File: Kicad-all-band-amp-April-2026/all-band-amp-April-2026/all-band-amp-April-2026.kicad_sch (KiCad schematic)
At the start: 120 parts, among them J1 SWR1, J10 Aux In, J11 LPF, J12 Digi In/Out, J13 12v/5v Outputs, J14 TX2/RX2, J15 TX0/RX0, J16 50v In., J17 PWM Out, J18 PTT IN, J19 DISPLAY POWER, J2 SWR2, J20 5V Output, J22 UDPI, J23 12v Output, J24 12v Output, J25 Temp 2, J26 Power Link, J3 I opt Input, J4 RF In Level, J5 50v In., J6 Temp, J7 Conn_01x03_Pin, J8 12v Input, J9 I2c Output, Q1 2n2222, Q2 2n2222, U1 LTV-847, U2 MCP23017_SP, U3 LM393, U4 MIC2981/82YN, U5 MIC2981/82YN, U6 R-78E5.0-1.0, U8 LTV-827, U9 ACS712xLCTR-30A

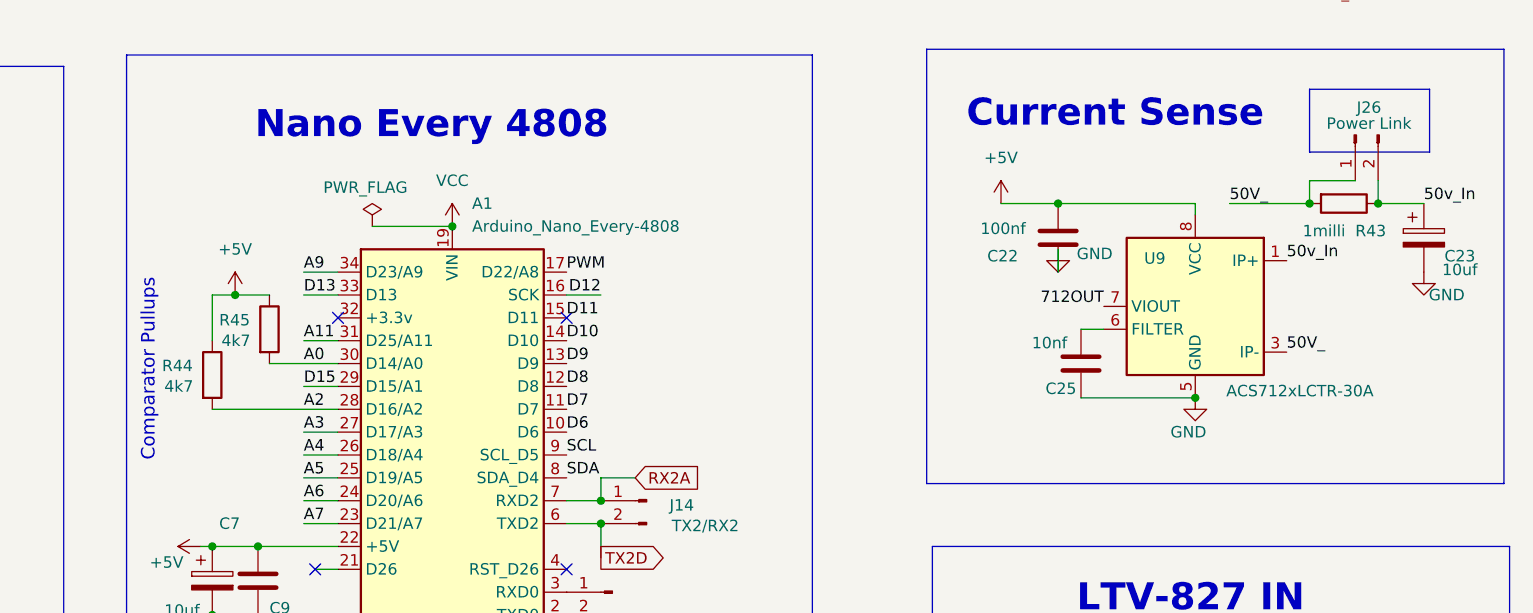
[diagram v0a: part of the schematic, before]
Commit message: change componet values
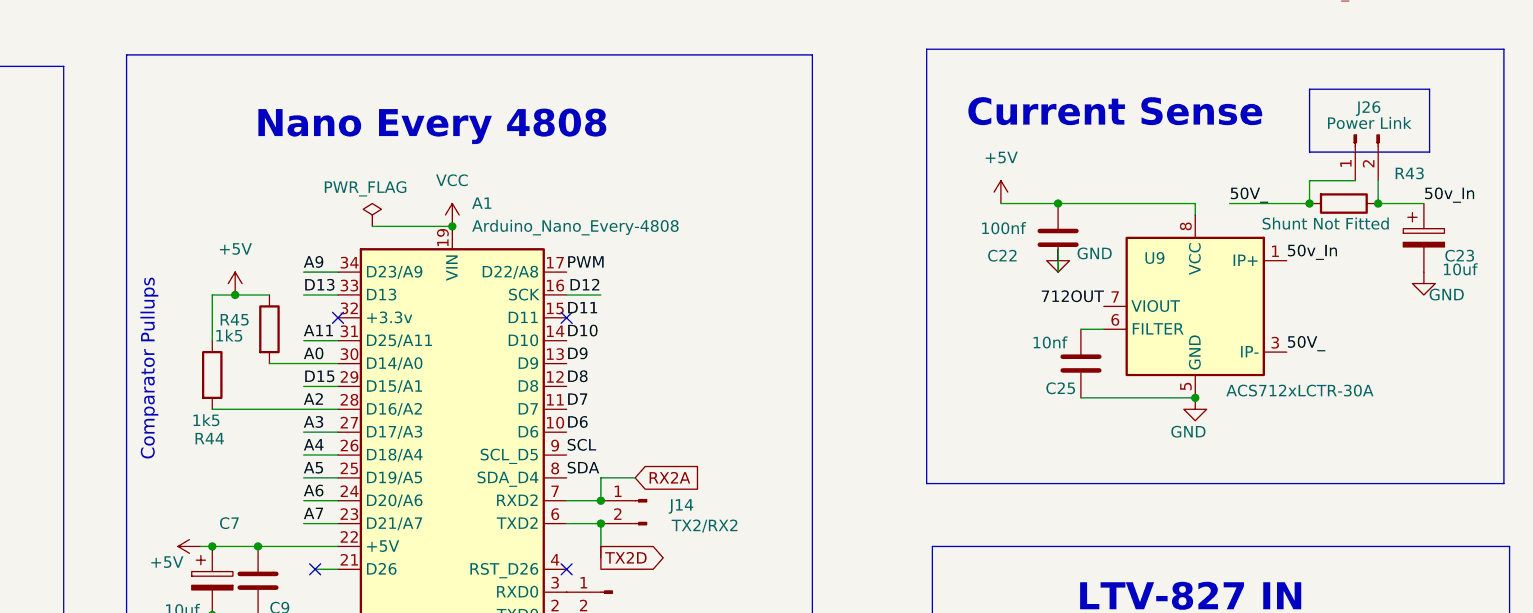
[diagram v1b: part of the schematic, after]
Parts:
- R43: value 1milli -> Shunt Not Fitted
- R44, R45: value 4k7 -> 1k5
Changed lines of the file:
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@@
 		(dnp no)
 		(property "Reference" "R44"
-			(at 252.222 87.884 0)
+			(at 255.778 96.012 0)
 			(effects
 				(font
@@
 			)
 		)
-		(property "Value" "4k7"
-			(at 252.476 90.17 0)
+		(property "Value" "1k5"
+			(at 255.524 93.98 0)
 			(effects
 				(font
@@
 			)
 		)
-		(property "Value" "4k7"
-			(at 258.826 85.09 0)
+		(property "Value" "1k5"
+			(at 258.064 84.582 0)
 			(effects
 				(font
@@
 		(dnp no)
 		(property "Reference" "R43"
-			(at 384.81 72.898 90)
+			(at 389.128 66.548 90)
 			(effects
 				(font
@@
 			)
 		)
-		(property "Value" "1milli"
-			(at 378.968 72.898 90)
+		(property "Value" "Shunt Not Fitted"
+			(at 374.396 72.136 90)
 			(effects
 				(font

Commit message: update functions
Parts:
- R3, R7: value 1k5 -> 1k5-3k3
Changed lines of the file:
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@@
 			)
 		)
-		(property "Value" "1k5"
-			(at 35.56 130.048 0)
+		(property "Value" "1k5-3k3"
+			(at 43.18 129.54 0)
 			(effects
 				(font
@@
 		(dnp no)
 		(property "Reference" "R7"
-			(at 36.83 175.006 0)
-			(effects
-				(font
-					(size 1.27 1.27)
-				)
-				(justify left)
-			)
-		)
-		(property "Value" "1k5"
-			(at 35.306 176.784 0)
-			(effects
-				(font
+			(at 36.576 176.53 0)
+			(effects
+				(font
+					(size 1.27 1.27)
+				)
+				(justify left)
+			)
+		)
+		(property "Value" "1k5-3k3"
+			(at 42.672 176.276 0)
+			(effects
+				(font

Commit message: improve display
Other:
- note added: "Note: Ensure only DC is applied to the RF in (drive) input. use a low pass filter. Dont let rf into the board!"
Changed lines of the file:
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@@
+		)
+	)
+	(text "Note: \nEnsure only DC is applied \nto the RF in (drive) input.\nuse a low pass filter.\nDont let rf into the board! "
+		(exclude_from_sim no)
+		(at 48.768 38.1 0)
+		(effects
+			(font
+				(size 3 3)
+				(thickness 0.6)
+				(bold yes)
+			)
 		)
 	)

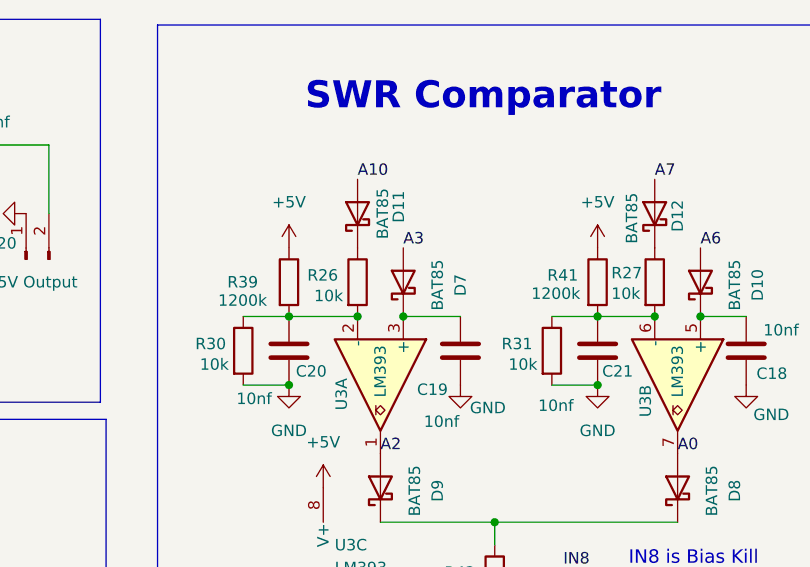
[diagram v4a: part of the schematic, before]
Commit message: update component values
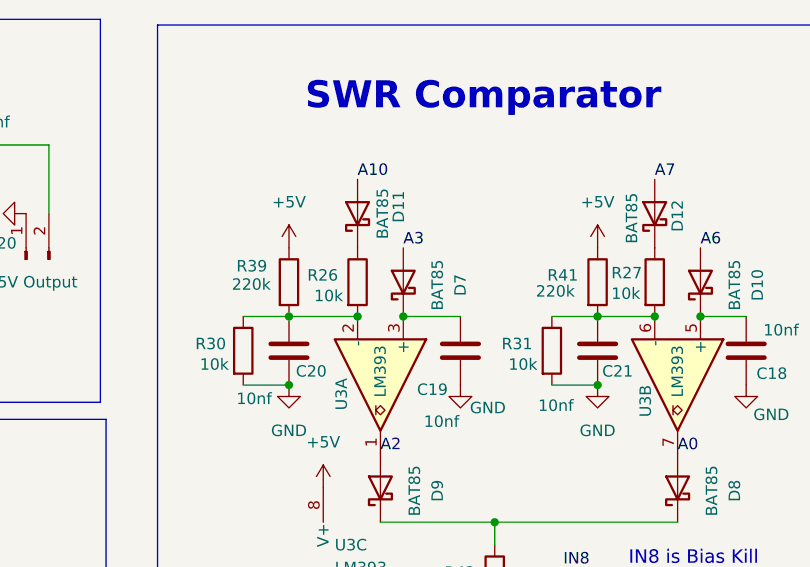
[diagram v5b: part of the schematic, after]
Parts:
- R39, R41: value 1200k -> 220k
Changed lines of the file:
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@@
 			)
 		)
-		(property "Value" "1200k"
-			(at 284.734 182.88 0)
+		(property "Value" "220k"
+			(at 285.242 182.626 0)
 			(show_name no)
 			(do_not_autoplace no)
@@
 		(dnp no)
 		(property "Reference" "R39"
-			(at 250.952 181.61 0)
+			(at 251.968 179.832 0)
 			(show_name no)
 			(do_not_autoplace no)
@@
 			)
 		)
-		(property "Value" "1200k"
-			(at 249.936 183.642 0)
+		(property "Value" "220k"
+			(at 251.46 181.864 0)
 			(show_name no)
 			(do_not_autoplace no)

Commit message: change some values - alter boards
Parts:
- R24, R25: value 10k -> 4k7
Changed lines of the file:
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@@
 			)
 		)
-		(property "Value" "10k"
+		(property "Value" "4k7"
 			(at 144.526 76.708 0)
 			(show_name no)
@@
 			)
 		)
-		(property "Value" "10k"
+		(property "Value" "4k7"
 			(at 131.826 78.74 0)
 			(show_name no)

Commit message: update pcb's
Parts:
- added C26: 10nf, Capacitor_THT:C_Disc_D3.4mm_W2.1mm_P2.50mm, symbol Device:C
- added J27: SWR trip out, Connector_JST:JST_EH_B2B-EH-A_1x02_P2.50mm_Vertical, symbol Connector:Conn_01x02_Pin
- added R46: 1k5, Resistor_THT:R_Axial_DIN0207_L6.3mm_D2.5mm_P7.62mm_Horizontal, symbol Device:R
- added R47: 1k, Resistor_THT:R_Axial_DIN0207_L6.3mm_D2.5mm_P7.62mm_Horizontal, symbol Device:R
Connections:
- net GND: now also C26.2, J27.1 (Pin_1), R47.2
- net SWR: now reaches J13.3 (Pin_3), U5.13 (OUT6), U5.14 (OUT5)
- net SWR: now also R46.2
- new net: C26.1, J27.2 (Pin_2), R46.1, R47.1
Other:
- note added: "SWR Trip out Protection Board etc."
- title: LDMOS Controller 2026 -> LDMOS Controller 2026 v2.10
- moved on the sheet: J12, J16, J17, J25, J5, J6, J9, Q1, R13, R14, R15, R34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
